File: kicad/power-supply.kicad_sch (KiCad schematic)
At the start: 29 parts, among them T1 BC846B, T10 BC846B, T3 BC846B, T4 BC856B, U4 LMR16006X

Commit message: pcb minor fixes, updated bom files, updated project name
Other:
- title: MPPT 2420 HC -> MPPT 4820 HC
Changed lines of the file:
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@@
   (paper "A4")
   (title_block
-    (title "MPPT 2420 HC")
+    (title "MPPT 4820 HC")
     (date "2021-01-06")
     (rev "0.2.3")

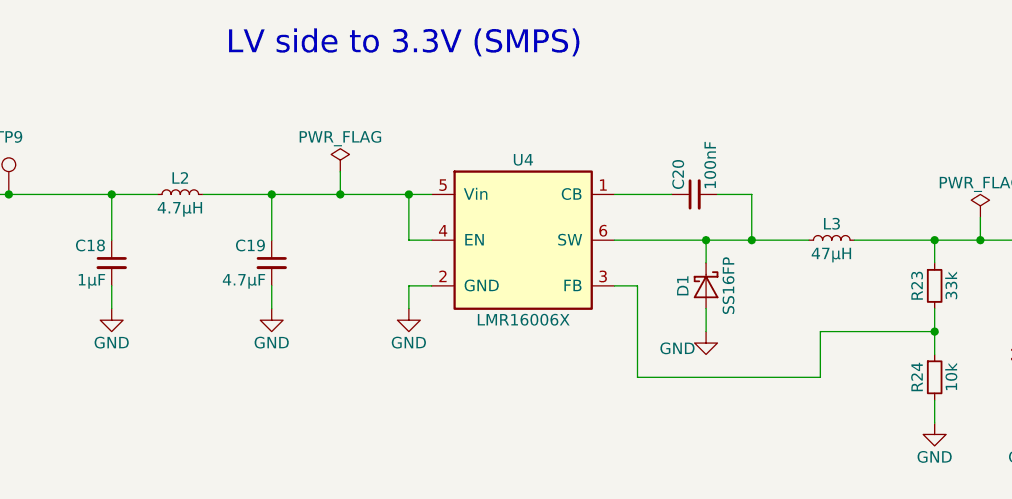
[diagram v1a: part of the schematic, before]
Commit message: updated project to kicad 7
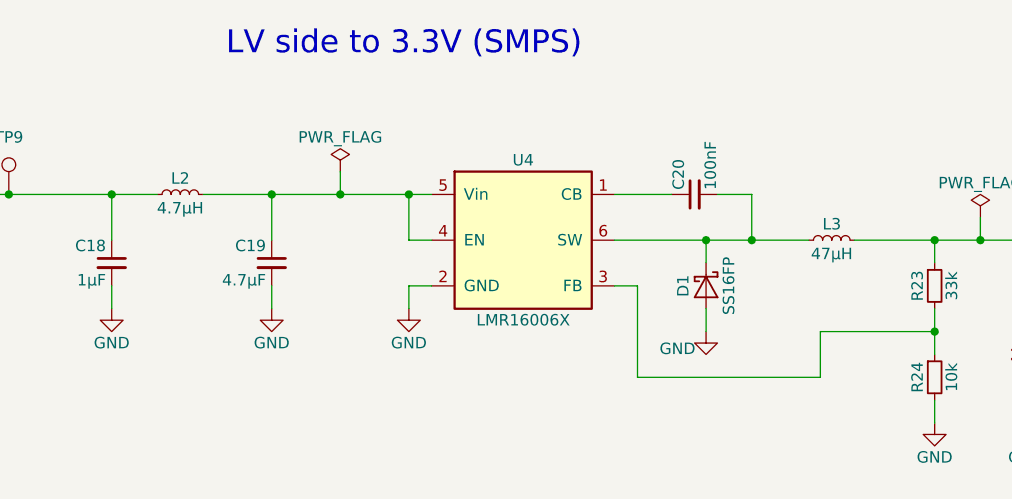
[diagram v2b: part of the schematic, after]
